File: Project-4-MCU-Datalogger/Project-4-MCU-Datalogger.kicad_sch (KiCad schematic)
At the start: 25 parts, among them U1 24LC1025, U2 24LC1025, U3 DS1337S_, U4 ATMEGA328P-AU, Y1 Crystal, Y2 Crystal

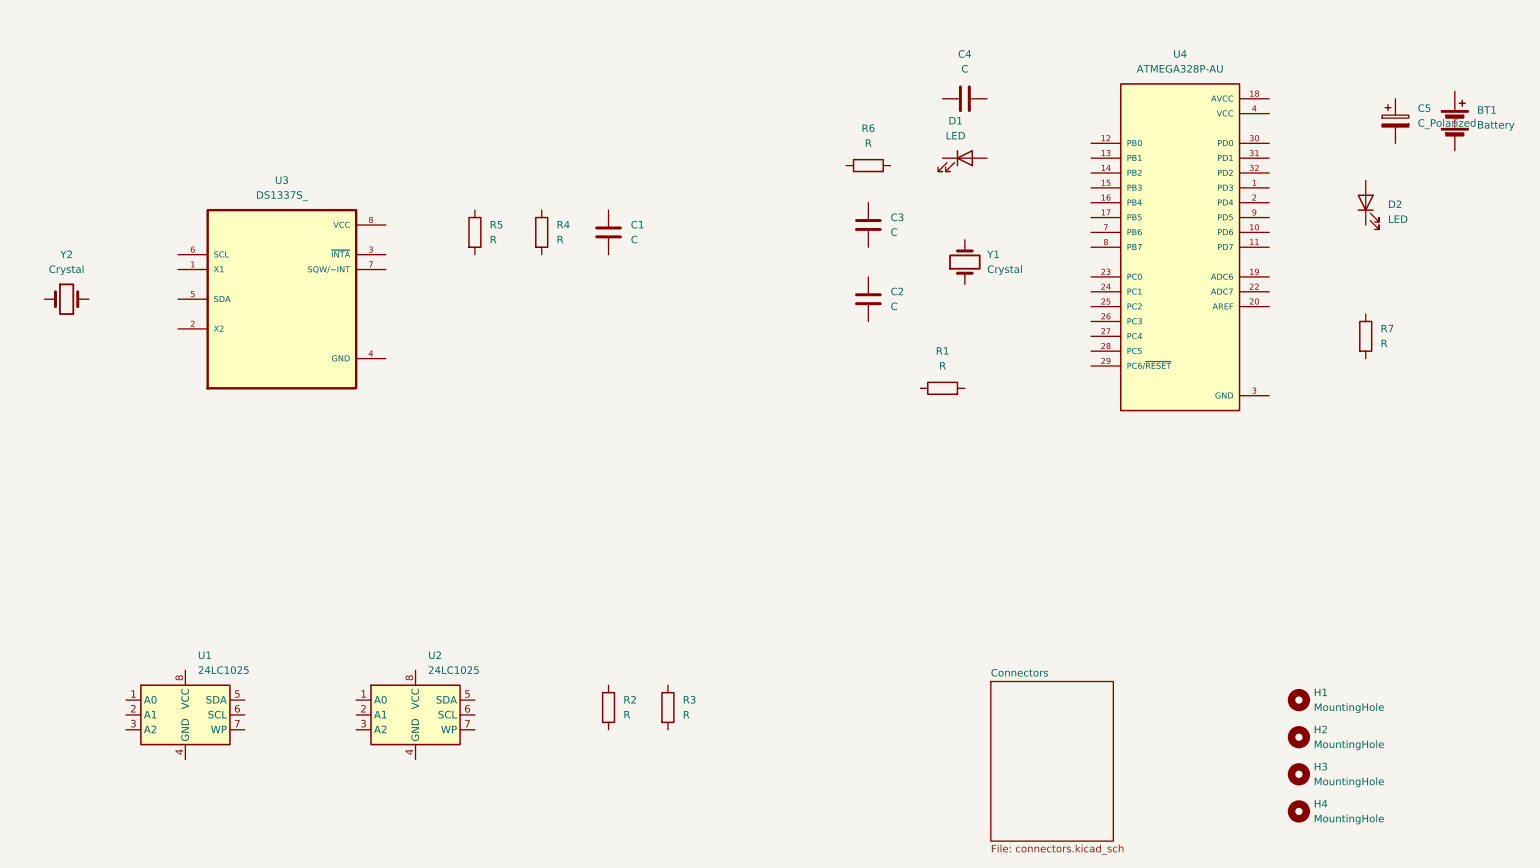
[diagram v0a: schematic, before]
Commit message: set symbols' values
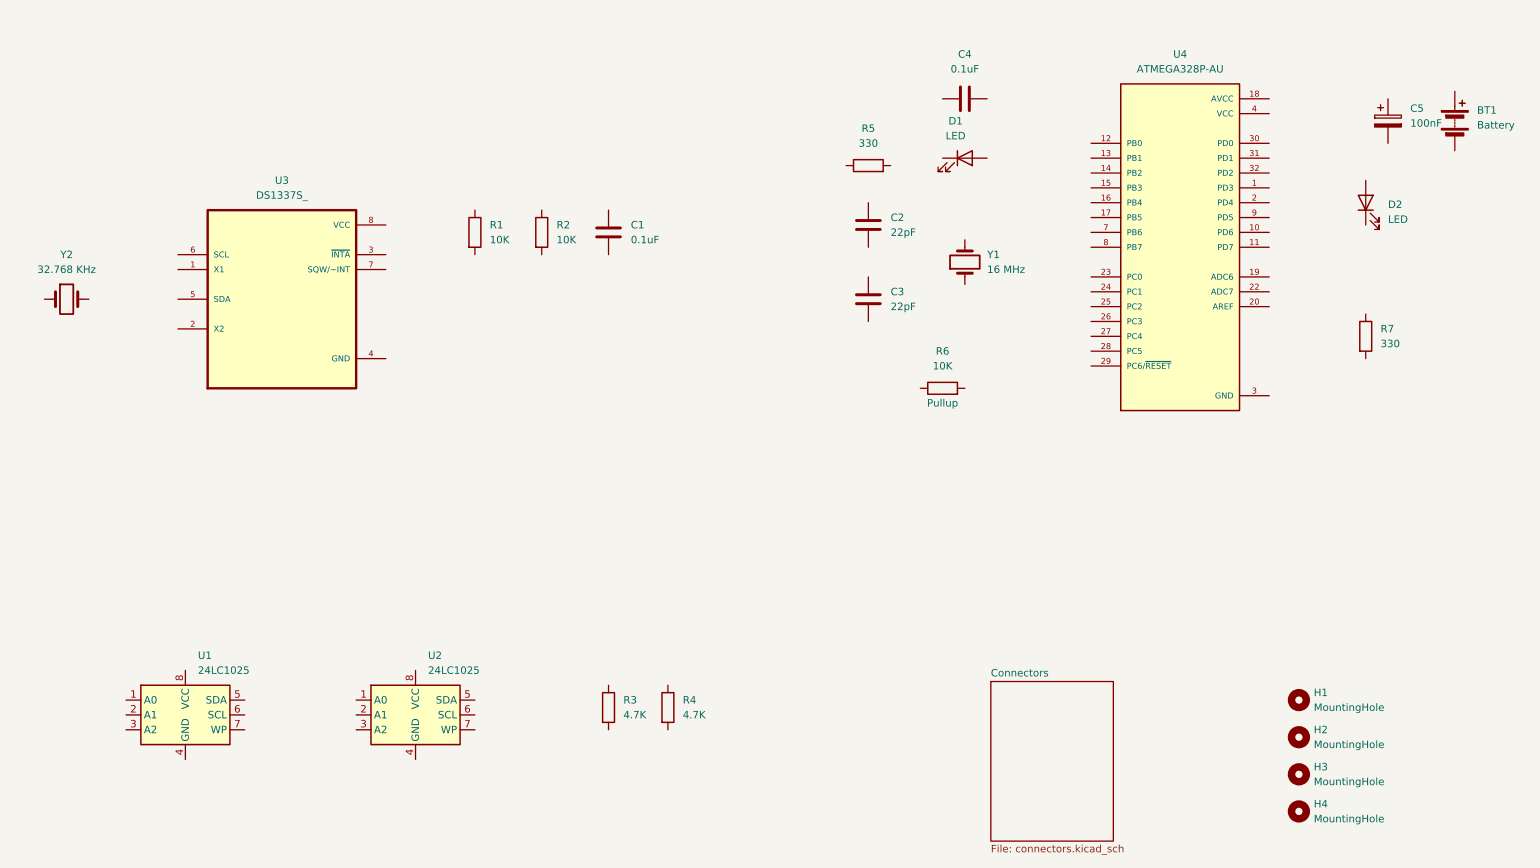
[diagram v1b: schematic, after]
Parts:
- C1, C4: value C -> 0.1uF
- C2: renamed from C3; value C -> 22pF
- C3: renamed from C2; value C -> 22pF
- C5: value C_Polarized -> 100nF
- R1: renamed from R5; value R -> 10K
- R2: renamed from R4; value R -> 10K
- R3: renamed from R2; value R -> 4.7K
- R4: renamed from R3; value R -> 4.7K
- R5: renamed from R6; value R -> 330
- R6: renamed from R1; value R -> 10K; Purpose (none) -> Pullup
- R7: value R -> 330
- Y1: value Crystal -> 16 MHz
- Y2: value Crystal -> 32.768 KHz
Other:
- moved on the sheet: C5

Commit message: assign footprints, inc imported footprints
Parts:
- BT1: footprint (none) -> Connector_PinHeader_2.54mm:PinHeader_1x02_P2.54mm_Vertical
- C1, C2, C3, C4, C5: footprint (none) -> Capacitor_SMD:C_0805_2012Metric
- D1, D2: footprint (none) -> LED_SMD:LED_0805_2012Metric
- H1, H2, H3, H4: footprint (none) -> MountingHole:MountingHole_2.1mm
- R1, R2, R3, R4, R5, R6, R7: footprint (none) -> Resistor_SMD:R_0805_2012Metric
- U1, U2: footprint (none) -> Package_SO:SOIC-8_5.3x5.3mm_P1.27mm
- Y1, Y2: footprint (none) -> Crystal:Crystal_SMD_5032-2Pin_5.0x3.2mm_HandSoldering
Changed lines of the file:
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@@
 			)
 		)
-		(property "Footprint" ""
+		(property "Footprint" "Capacitor_SMD:C_0805_2012Metric"
 			(at 190.5 33.3248 0)
 			(hide yes)
@@
 			)
 		)
-		(property "Footprint" ""
+		(property "Footprint" "MountingHole:MountingHole_2.1mm"
 			(at 243.84 156.21 0)
 			(hide yes)
@@
 			)
 		)
-		(property "Footprint" ""
+		(property "Footprint" "MountingHole:MountingHole_2.1mm"
 			(at 243.84 143.51 0)
 			(hide yes)
@@
 			)
 		)
-		(property "Footprint" ""
+		(property "Footprint" "Resistor_SMD:R_0805_2012Metric"
 			(at 170.18 47.498 90)
 			(hide yes)
@@
 			)
 		)
-		(property "Footprint" ""
+		(property "Footprint" "MountingHole:MountingHole_2.1mm"
 			(at 243.84 149.86 0)
 			(hide yes)
@@
 			)
 		)
-		(property "Footprint" ""
+		(property "Footprint" "LED_SMD:LED_0805_2012Metric"
 			(at 255.27 52.07 0)
 			(hide yes)
@@
 			)
 		)
-		(property "Footprint" ""
+		(property "Footprint" "Resistor_SMD:R_0805_2012Metric"
 			(at 134.112 138.43 90)
 			(hide yes)
@@
 			)
 		)
-		(property "Footprint" ""
+		(property "Footprint" "Crystal:Crystal_SMD_5032-2Pin_5.0x3.2mm_HandSoldering"
 			(at 33.02 68.58 0)
 			(hide yes)
@@
 			)
 		)
-		(property "Footprint" ""
+		(property "Footprint" "MountingHole:MountingHole_2.1mm"
 			(at 243.84 137.16 0)
 			(hide yes)
@@
 			)
 		)
-		(property "Footprint" ""
+		(property "Footprint" "Resistor_SMD:R_0805_2012Metric"
 			(at 101.092 57.15 90)
 			(hide yes)
@@
 			)
 		)
-		(property "Footprint" ""
+		(property "Footprint" "Package_SO:SOIC-8_5.3x5.3mm_P1.27mm"
 			(at 92.71 139.7 0)
 			(hide yes)
@@
 			)
 		)
-		(property "Footprint" ""
+		(property "Footprint" "Capacitor_SMD:C_0805_2012Metric"
 			(at 171.1452 59.69 0)
 			(hide yes)
@@
 			)
 		)
-		(property "Footprint" ""
+		(property "Footprint" "Resistor_SMD:R_0805_2012Metric"
 			(at 182.88 85.598 90)
 			(hide yes)
@@
 			)
 		)
-		(property "Footprint" ""
+		(property "Footprint" "Resistor_SMD:R_0805_2012Metric"
 			(at 123.952 138.43 90)
 			(hide yes)
@@
 			)
 		)
-		(property "Footprint" ""
+		(property "Footprint" "Connector_PinHeader_2.54mm:PinHeader_1x02_P2.54mm_Vertical"
 			(at 270.51 36.576 90)
 			(hide yes)
@@
 			)
 		)
-		(property "Footprint" ""
+		(property "Footprint" "Crystal:Crystal_SMD_5032-2Pin_5.0x3.2mm_HandSoldering"
 			(at 186.69 62.23 0)
 			(hide yes)
@@
 			)
 		)
-		(property "Footprint" ""
+		(property "Footprint" "Capacitor_SMD:C_0805_2012Metric"
 			(at 171.1452 72.39 0)
 			(hide yes)
@@
 			)
 		)
-		(property "Footprint" ""
+		(property "Footprint" "LED_SMD:LED_0805_2012Metric"
 			(at 186.69 44.45 0)
 			(hide yes)
@@
 			)
 		)
-		(property "Footprint" ""
+		(property "Footprint" "Capacitor_SMD:C_0805_2012Metric"
 			(at 126.6952 60.96 0)
 			(hide yes)
@@
 			)
 		)
-		(property "Footprint" ""
+		(property "Footprint" "Resistor_SMD:R_0805_2012Metric"
 			(at 112.522 57.15 90)
 			(hide yes)
@@
 			)
 		)
-		(property "Footprint" ""
+		(property "Footprint" "Resistor_SMD:R_0805_2012Metric"
 			(at 253.492 74.93 90)
 			(hide yes)
@@
 			)
 		)
-		(property "Footprint" ""
+		(property "Footprint" "Package_SO:SOIC-8_5.3x5.3mm_P1.27mm"
 			(at 53.34 139.7 0)
 			(hide yes)
@@
 			)
 		)
-		(property "Footprint" ""
+		(property "Footprint" "Capacitor_SMD:C_0805_2012Metric"
 			(at 260.0452 41.91 0)
 			(hide yes)

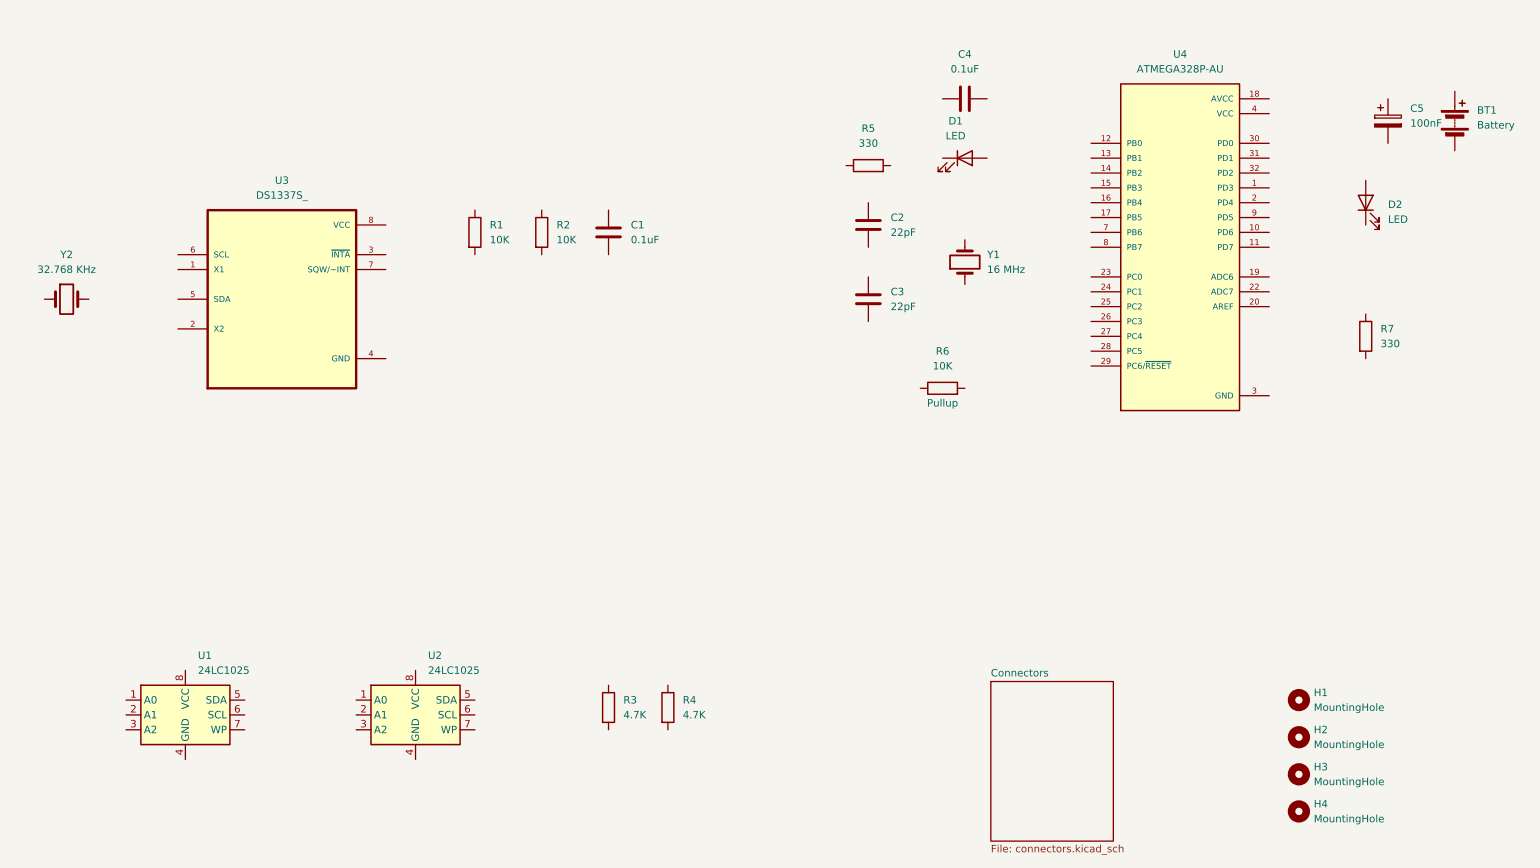
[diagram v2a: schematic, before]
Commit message: wire main sheet
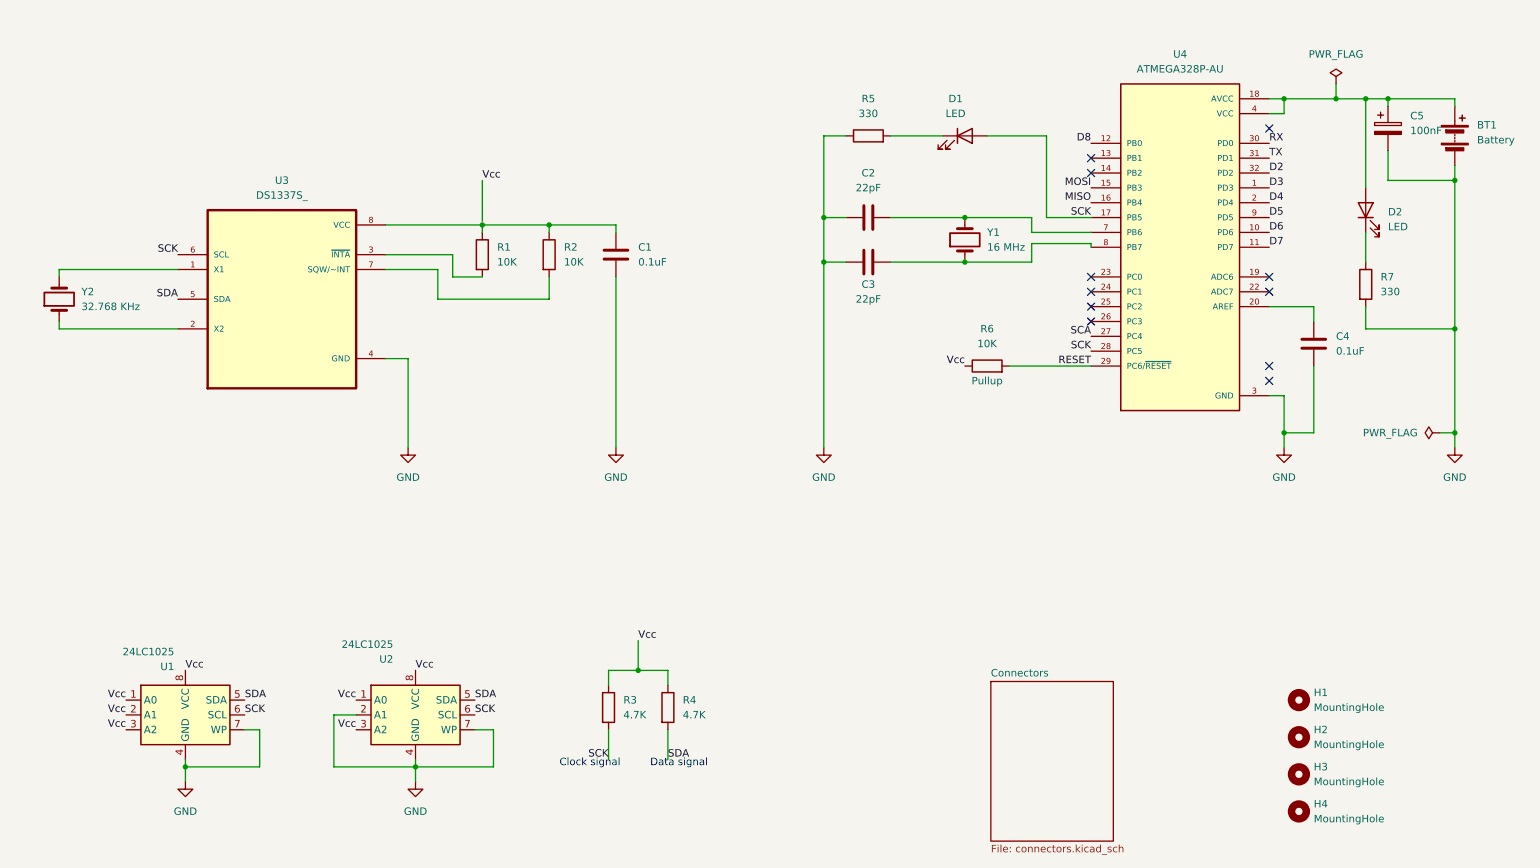
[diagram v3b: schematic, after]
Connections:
- net GND: now also BT1.2 (-), C1.2, C2.1, C3.1, C4.1, C5.2, R5.1, R7.2, U1.4 (GND), U1.7 (WP), U2.2 (A1), U2.4 (GND), U2.7 (WP), U3.4 (GND)
- net VCC: no longer U4.4 (VCC)
- net at C4.2: now also U4.20 (AREF)
- net D3: now reaches U4.1 (PD3)
- net D6: now reaches U4.10 (PD6)
- net D7: now reaches U4.11 (PD7)
- net D8: now reaches U4.12 (PB0)
- net MOSI: now reaches U4.15 (PB3)
- net MISO: now reaches U4.16 (PB4)
- net SCK: now reaches U4.17 (PB5)
- net SCK: now also D1.2 (A), R3.2, U1.6 (SCL), U2.6 (SCL), U3.6 (SCL), U4.28 (PC5)
- net at U4.18 (AVCC): now also BT1.1 (+), C5.1, D2.2 (A), U4.4 (VCC)
- net D4: now reaches U4.2 (PD4)
- net SCA: now reaches U4.27 (PC4)
- net RESET: now reaches U4.29 (PC6/~{RESET})
- net RESET: now also R6.2
- net RX: now reaches U4.30 (PD0)
- net TX: now reaches U4.31 (PD1)
- net D2: now reaches U4.32 (PD2)
- net at U4.7 (PB6): now also C2.2, Y1.2
- net at U4.8 (PB7): now also C3.2, Y1.1
- net D5: now reaches U4.9 (PD5)
- net at R5.2: now also D1.1 (K)
- net at U3.1 (X1): now also Y2.2
- net at U3.2 (X2): now also Y2.1
- net at U3.3 (~{INTA}): now also R1.2
- net SDA: now reaches U3.5 (SDA)
- net SDA: now also R4.2, U1.5 (SDA), U2.5 (SDA)
- net at U3.7 (SQW/~INT): now also R2.2
- net at U3.8 (VCC): now also C1.1, R1.1, R2.1
- net at D2.1 (K): now also R7.1
- net Vcc: now reaches R4.1
- net Vcc: now also R3.1, R6.1, U1.1 (A0), U1.2 (A1), U1.3 (A2), U1.8 (VCC), U2.1 (A0), U2.3 (A2), U2.8 (VCC)
- no-connect marks 0 -> 11
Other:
- note added: "Clock signal"
- note added: "Data signal"
- moved on the sheet: BT1, C1, C2, C3, C4, C5, D1, D2, R1, R2, R5, R6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

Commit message: wire hierarchical child sheet, add hierarchical labels, connect sheets, run ERC
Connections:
- net SCA is gone; now on net SDA: U4.27 (PC4)
- net Vcc: now also C1.1, R1.1, R2.1, U3.8 (VCC)
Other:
- sheet Connectors ports: added D2, D3, D4, D5, D6, D7, D8, GND, MISO, MOSI, RESET, RX, SCK, SDA, TX, Vcc; removed none

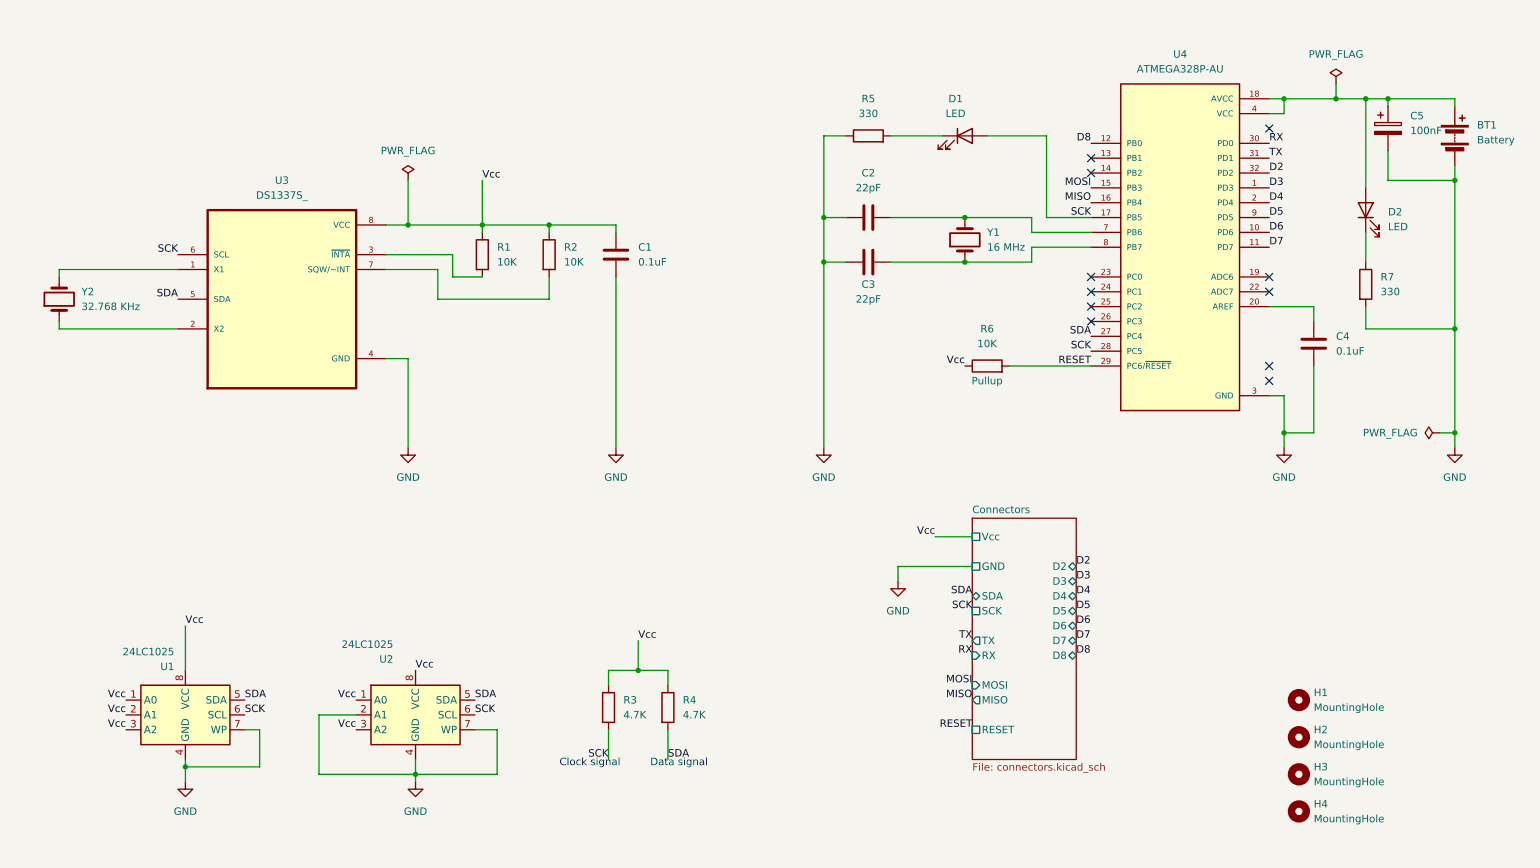
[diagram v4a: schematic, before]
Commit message: add boxes and comments for clarity
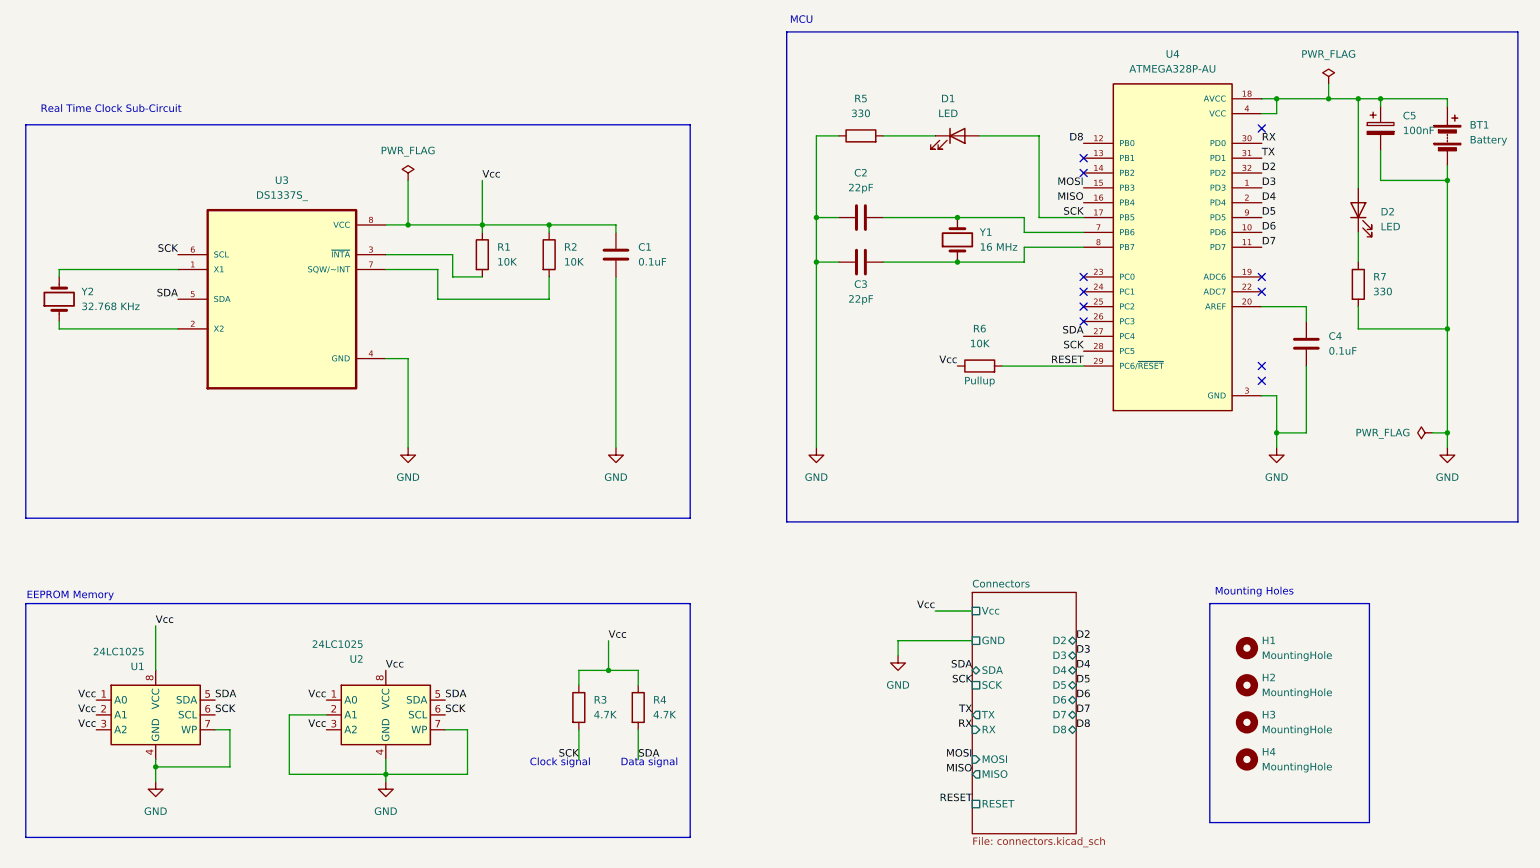
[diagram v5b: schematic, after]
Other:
- note added: "EEPROM Memory"
- note added: "MCU"
- note added: "Mounting Holes"
- note added: "Real Time Clock Sub-Circuit"
- moved on the sheet: BT1, C2, C3, C4, C5, D1, D2, H1, H2, H3, H4, R3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
